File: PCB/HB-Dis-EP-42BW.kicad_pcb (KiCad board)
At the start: 2 copper layers, 30 parts, among them J1 Reset, J2 FTDI, J4 ePaper, J6 Supply, SW0 SW_Push, SW1 SW_Push, SW10 SW_Push, SW2 SW_Push, SW3 SW_Push, SW4 SW_Push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

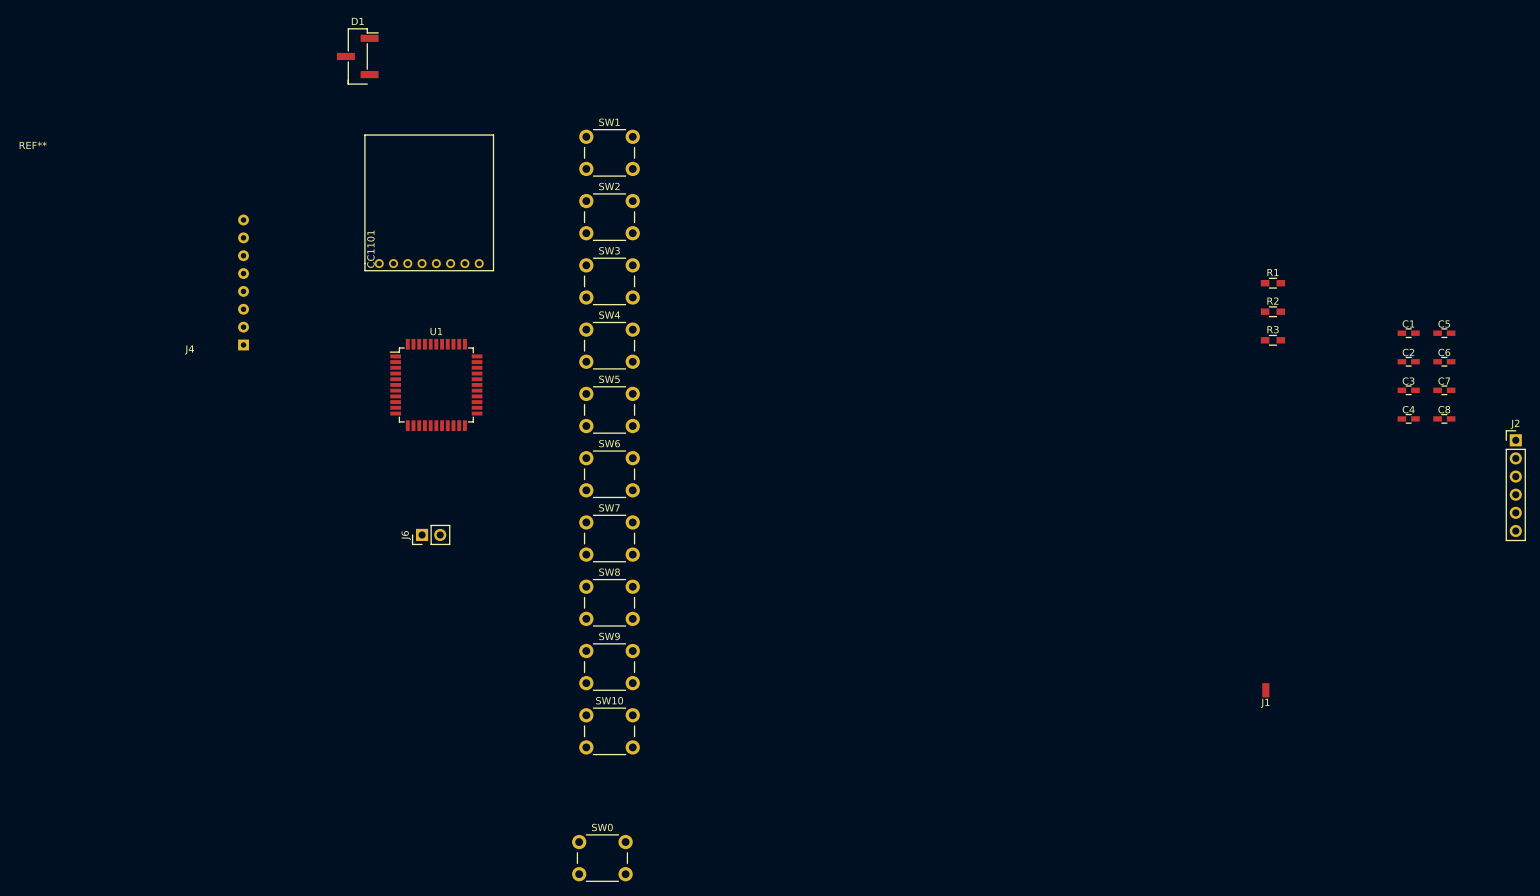
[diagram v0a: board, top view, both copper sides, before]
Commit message: initial PCB placement
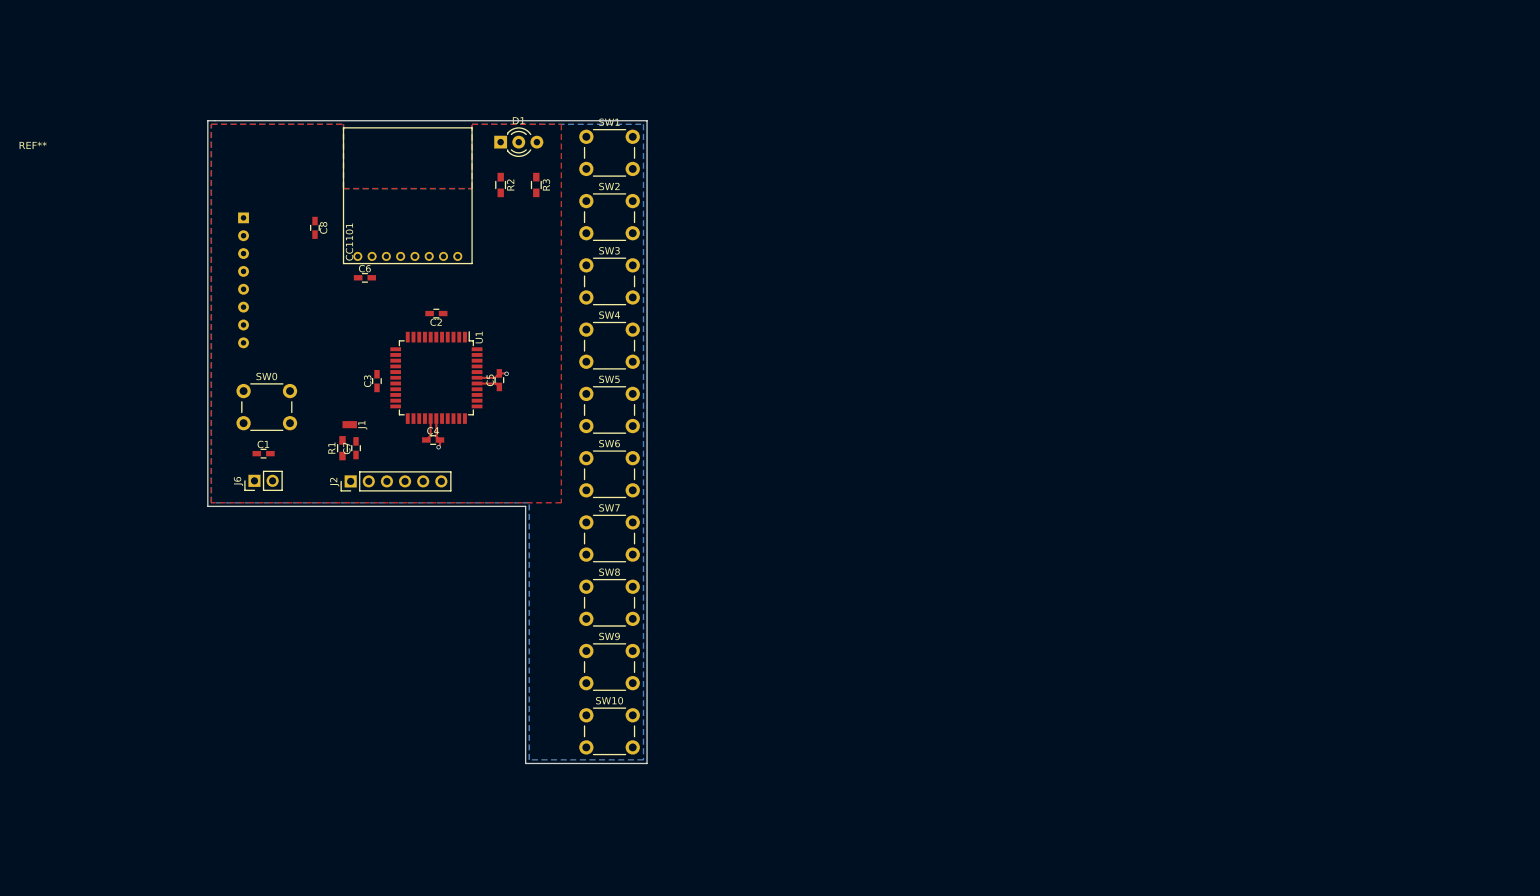
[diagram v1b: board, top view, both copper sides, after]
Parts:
- D1: value LED_Dual_AAC -> LED_Dual; footprint Pin_Headers:Pin_Header_Straight_1x03_Pitch2.54mm_SMD_Pin1Right -> LEDs:LED_D3.0mm-3
- J4: moved to B.Cu
- moved J2 163.2 mm to (79.0, 90.5), turned to 90 degrees
- moved C1 161.2 mm to (66.8, 86.6)
- moved C8 160.4 mm to (74.0, 55.0), turned to 270 degrees
- moved C7 152.6 mm to (79.8, 85.9), turned to 90 degrees
- moved C6 151.6 mm to (81.0, 62.0)
- moved C3 144.5 mm to (82.7, 76.5), turned to 90 degrees
- moved C4 136.6 mm to (90.6, 84.7)
- moved C2 136.3 mm to (91.0, 67.0), turned to 180 degrees
- moved J1 133.6 mm to (78.9, 82.6), turned to 90 degrees
- moved C5 132.5 mm to (99.8, 76.3), turned to 90 degrees
- moved R1 132.3 mm to (77.9, 85.9), turned to 90 degrees
- moved R2 109.6 mm to (100.0, 49.0), turned to 270 degrees
- moved R3 105.4 mm to (105.0, 49.0), turned to 270 degrees
- moved SW0 78.7 mm to (64.0, 77.9)
- moved J6 24.7 mm to (65.5, 90.4)
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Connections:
- D1 pad 2: Net-(D1-Pad2) -> GND
- D1 pad 3: GND -> Net-(D1-Pad3)
- R2 pad 1: Net-(D1-Pad2) -> Net-(D1-Pad1)
- R2 pad 2: /LED2 -> /LED1
- R3 pad 1: Net-(D1-Pad1) -> Net-(D1-Pad3)
- R3 pad 2: /LED1 -> /LED2
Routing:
- net GND: track 0.00 -> 8.73 mm, vias 0 -> 2
- net VCC: track 0.00 -> 6.58 mm
- added copper zone on B.Cu, net GND
- added copper zone on F.Cu, net VCC
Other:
- board outline added: 61.5 x 90 mm
- rule trace_min: 0.2 -> 0.25
- board text added: "SMD button?"
- board text added: "red/green LED"

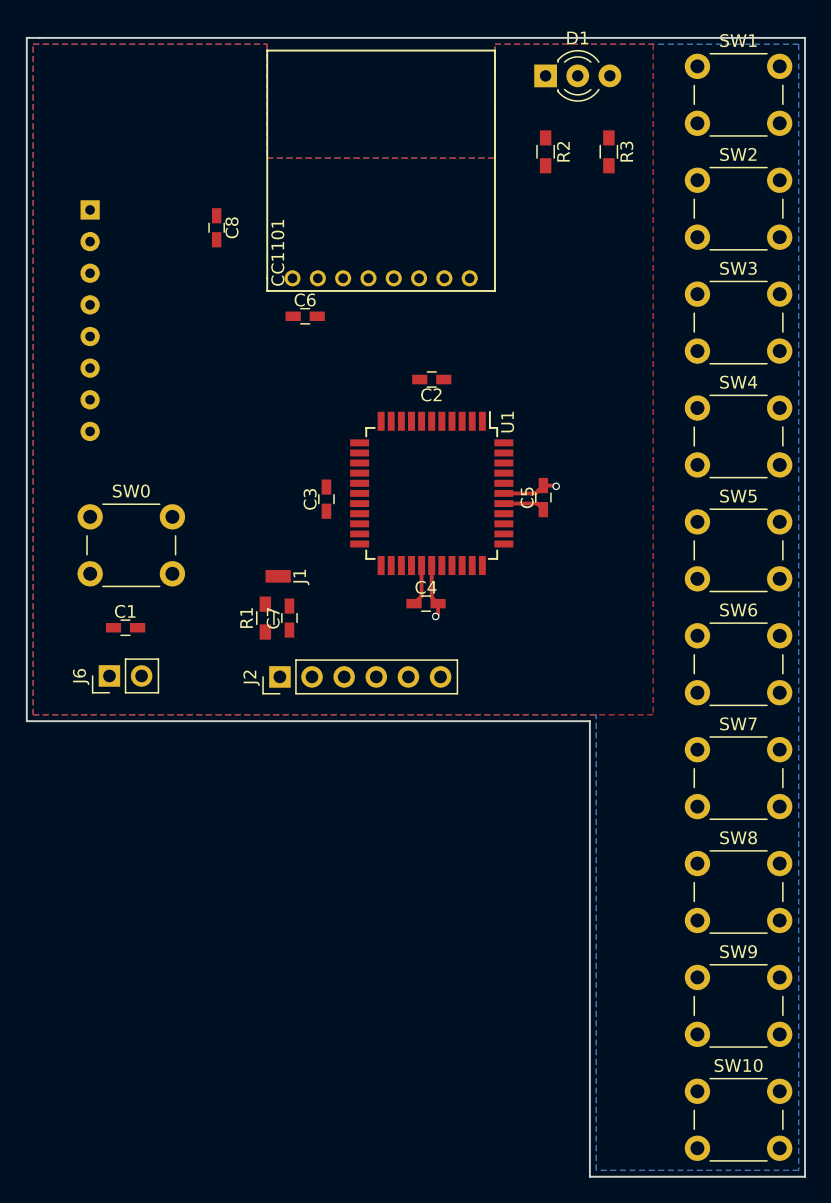
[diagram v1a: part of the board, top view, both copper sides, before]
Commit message: routing...
- moved decoupling caps to bottom side
- routed most of it
- looks like the button pins shall be rearranged for better routing
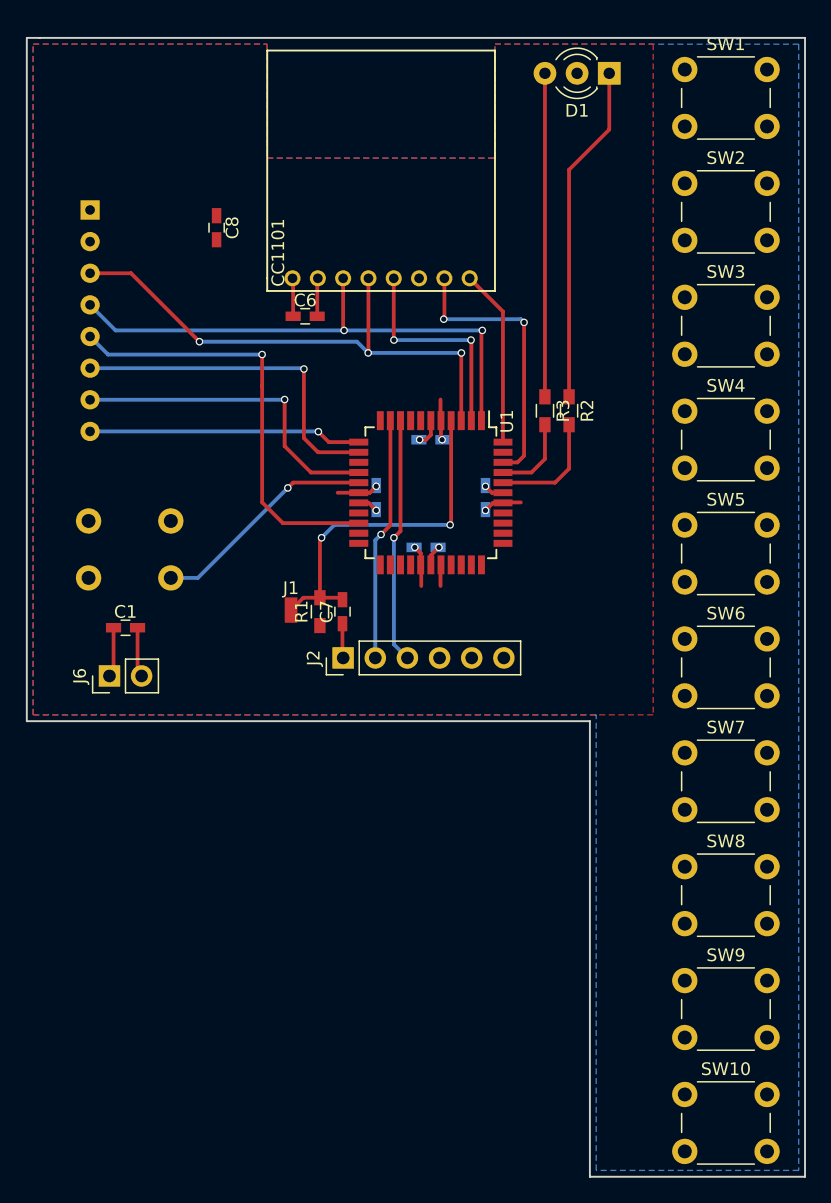
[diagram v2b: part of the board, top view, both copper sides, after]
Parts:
- C2, C3, C4, C5, SW0: moved to B.Cu
- moved R3 21.1 mm to (99.9, 69.5)
- moved R2 20.6 mm to (101.9, 69.5)
- moved J2 5.22 mm to (84.0, 89.0)
- moved D1 5.03 mm to (105.0, 42.8), turned to 180 degrees
- moved SW0 4.83 mm to (63.9, 82.7)
- moved C2 4.76 mm to (90.9, 71.8)
- moved C5 4.57 mm to (95.3, 76.3)
- moved C4 4.44 mm to (90.6, 80.3)
- moved R1 4.35 mm to (82.2, 85.3)
- moved C7 4.22 mm to (83.9, 85.3)
- moved C3 3.94 mm to (86.6, 76.3), turned to 270 degrees
- moved J1 2.85 mm to (79.9, 85.2), turned to 180 degrees
- moved SW1 1.03 mm to (111.0, 42.5)
- moved SW10 1.03 mm to (111.0, 123.5)
- moved SW2 1.03 mm to (111.0, 51.5)
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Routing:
- net /SCK: track 0.00 -> 43.2 mm, vias 0 -> 3
- net /MOSI: track 0.00 -> 43.1 mm, vias 0 -> 2
- net /GxCS: track 0.00 -> 34.3 mm, vias 0 -> 1
- net /RESET: track 0.00 -> 28.2 mm, vias 0 -> 2
- net /GxDC: track 0.00 -> 27.2 mm, vias 0 -> 1
- net Net-(D1-Pad1): track 0.00 -> 26.9 mm
- net /GxRST: track 0.00 -> 25.8 mm, vias 0 -> 1
- net Net-(D1-Pad3): track 0.00 -> 25.6 mm
- net /GDO0: track 0.00 -> 22.1 mm, vias 0 -> 2
- net /GxBSY: track 0.00 -> 21.6 mm, vias 0 -> 1
- net /RX: track 0.00 -> 19.4 mm, vias 0 -> 1
- net /TX: track 0.00 -> 19.2 mm, vias 0 -> 1
- net /CONFIG: track 0.00 -> 18.0 mm, vias 0 -> 1
- net /MISO: track 0.00 -> 17.4 mm, vias 0 -> 2
- net VCC: track 6.58 -> 21.7 mm, vias 0 -> 4
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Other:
- board text added: "8.5 mm spacing between buttons"

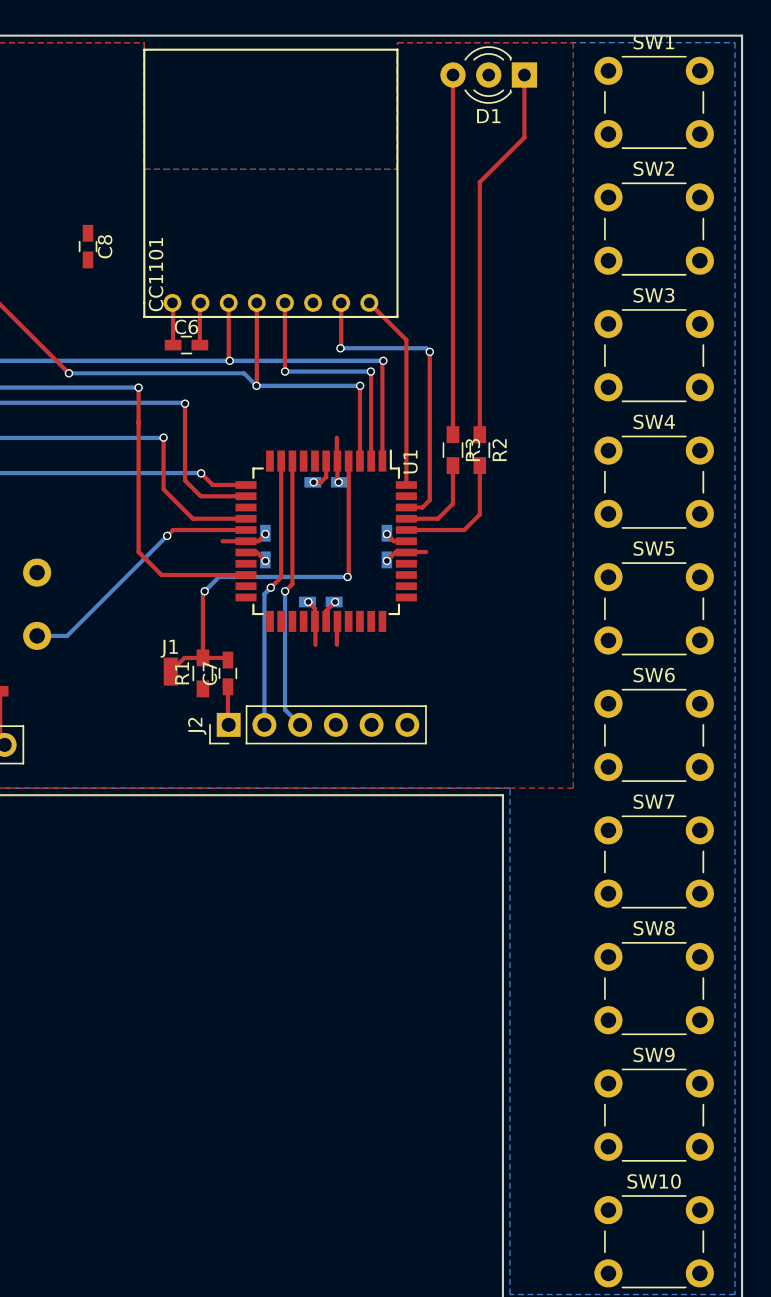
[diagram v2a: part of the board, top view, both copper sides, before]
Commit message: first board layout done, buttons swapped
buttons are connected differently to simplify routing
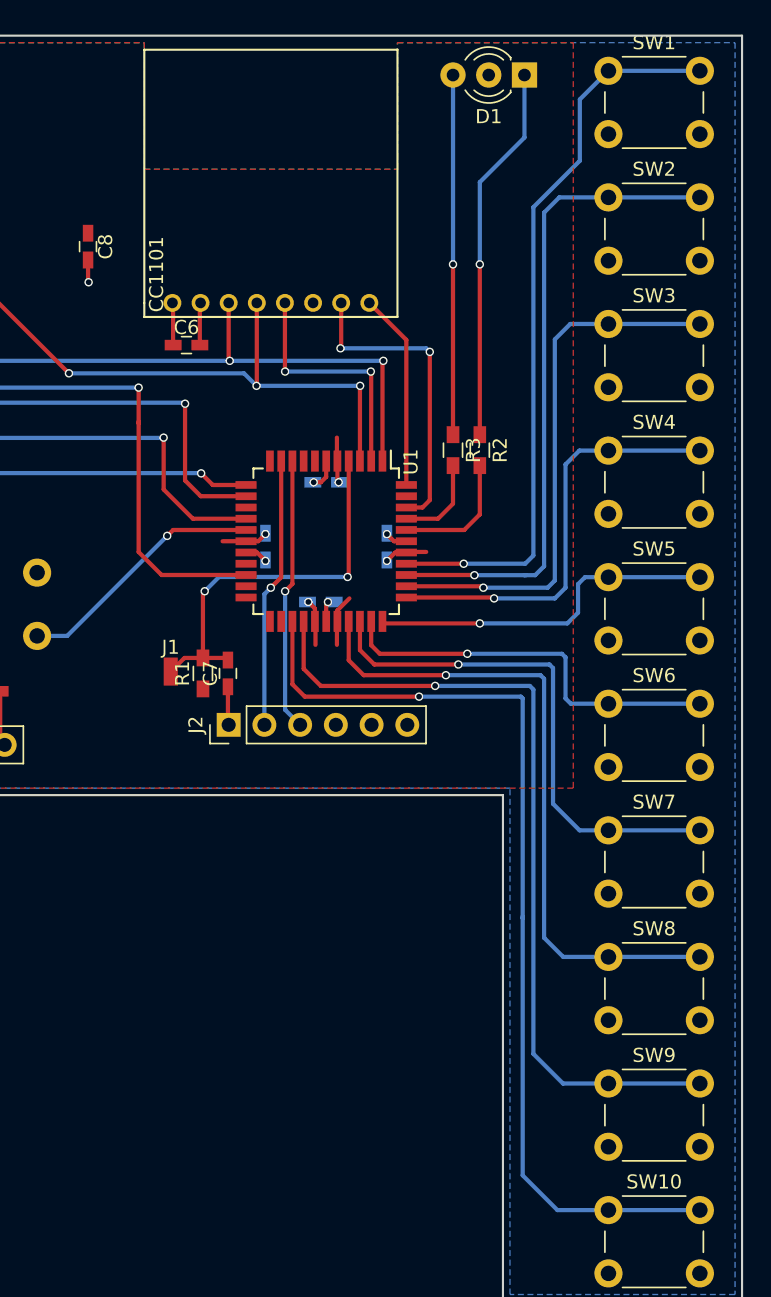
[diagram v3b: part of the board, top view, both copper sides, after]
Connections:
- U1 pad 25: /BTN9 -> /BTN10
- U1 pad 26: /BTN10 -> /BTN9
- U1 pad 30: /BTN1 -> /BTN8
- U1 pad 31: /BTN2 -> /BTN7
- U1 pad 32: /BTN3 -> /BTN6
- U1 pad 33: /BTN4 -> /BTN5
- U1 pad 34: /BTN5 -> /BTN4
- U1 pad 35: /BTN6 -> /BTN3
- U1 pad 36: /BTN7 -> /BTN2
- U1 pad 37: /BTN8 -> /BTN1
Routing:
- net /BTN10: track 0.00 -> 68.9 mm, vias 0 -> 1
- net /BTN9: track 0.00 -> 58.9 mm, vias 0 -> 1
- net /BTN1: track 0.00 -> 52.5 mm, vias 0 -> 1
- net /BTN8: track 0.00 -> 47.3 mm, vias 0 -> 1
- net /BTN2: track 0.00 -> 46.9 mm, vias 0 -> 1
- net /BTN3: track 0.00 -> 38.7 mm, vias 0 -> 1
- net /BTN7: track 0.00 -> 37.2 mm, vias 0 -> 1
- net /BTN4: track 0.00 -> 30.4 mm, vias 0 -> 1
- net /BTN6: track 0.00 -> 28.5 mm, vias 0 -> 1
- net /BTN5: track 0.00 -> 25.2 mm, vias 0 -> 1
- net GND: track 14.3 -> 16.8 mm, vias 4 -> 5
- net VCC: track 21.7 -> 23.7 mm
- net Net-(D1-Pad3): vias 0 -> 1
- net Net-(D1-Pad1): vias 0 -> 1
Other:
- board text added: "config button on backside drill small hole in the back of the case"
- board text removed: "SMD button?"
